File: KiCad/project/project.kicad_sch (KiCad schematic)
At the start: 15 parts, among them P1 Header-Female-2.54_1x3, U1 DRV8313PWPR

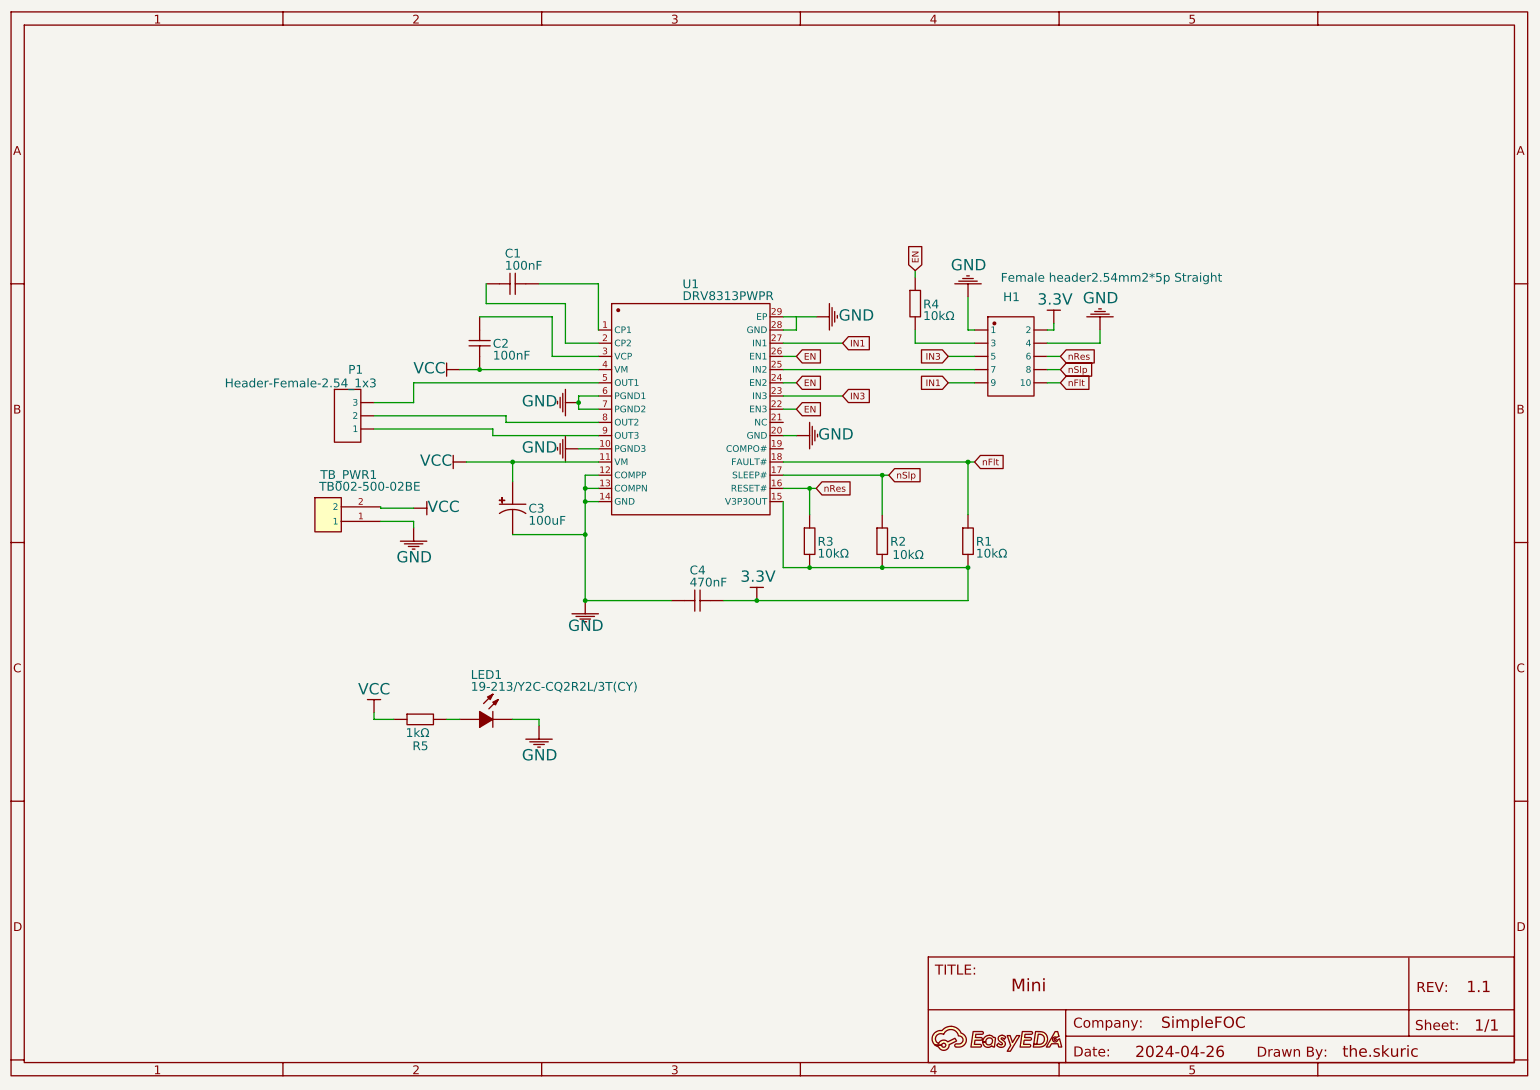
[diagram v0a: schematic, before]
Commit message: Remove imported EasyEDA drawing-frame placeholder from schematic
The EasyEDA import brought in the sheet border/title-block as an
unresolved 291x204mm placeholder symbol (lib_id Unknown_0_-806, ref A1)
wrapping the whole schematic — ~1360 lines / 70KB of non-functional
graphics. KiCad provides its own sheet frame, so it's removed.
Schematic still parses; ERC lib_symbol_issues 30 -> 29.

Co-Authored-By: Claude Opus 4.8 (1M context) <noreply@anthropic.com>
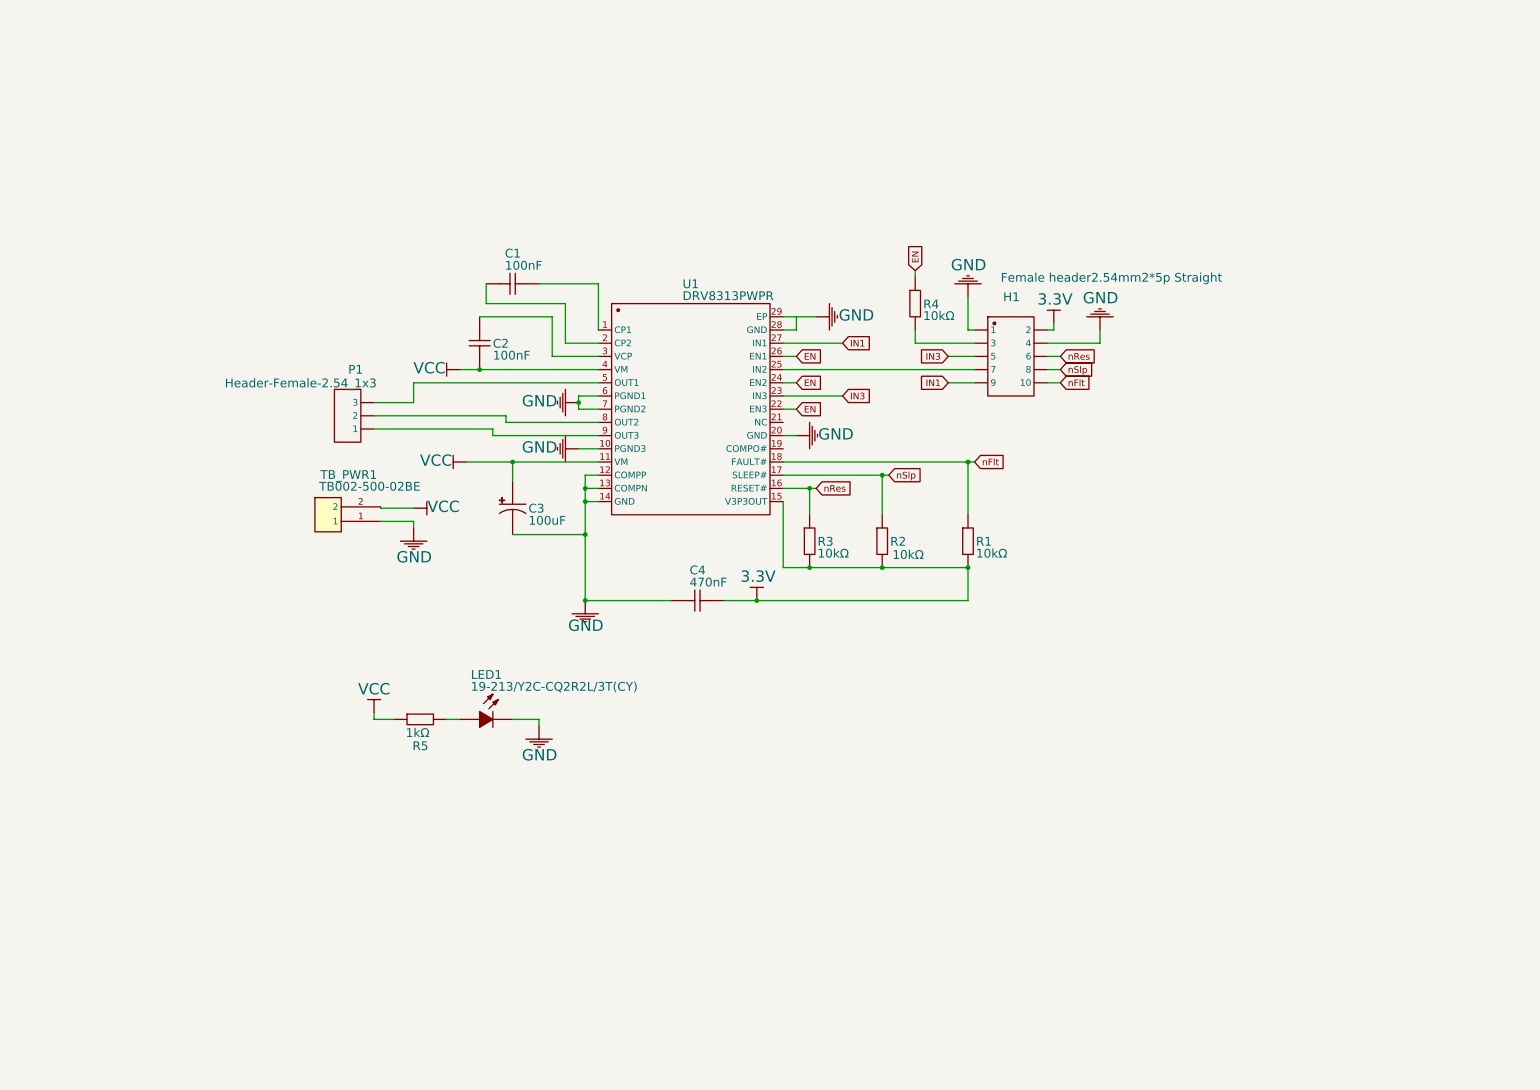
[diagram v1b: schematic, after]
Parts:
- removed A1: A, symbol Unknown_0_-806
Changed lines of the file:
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@@
-		)
-	)
-	(symbol
-		(lib_id "Unknown_0_-806")
-		(at 0 -0.254 0)
-		(unit 0)
-		(body_style 0)
-		(exclude_from_sim no)
-		(in_bom yes)
-		(on_board yes)
-		(in_pos_files yes)
-		(dnp no)
-		(property "Reference" "A1"
-			(at 144.9578 -4.8641 0)
-			(hide yes)
-			(show_name no)
-			(do_not_autoplace no)
-			(effects
-				(font
-					(face "Arial")
-					(size 1.6891 1.6891)
-				)
-				(justify left top)
-			)
-		)
-		(property "Value" "A"
-			(at 144.9578 -2.7051 0)
-			(hide yes)
-			(show_name no)
-			(do_not_autoplace no)
-			(effects
-				(font
-					(face "Arial")
-					(size 1.6891 1.6891)
-				)
-				(justify left top)
-			)
-		)
-		(property "Footprint" ""
-			(at 0 -0.254 0)
-			(hide yes)
-			(show_name no)
-			(do_not_autoplace no)
-			(effects
-				(font
-					(size 1.27 1.27)
-				)
-			)
-		)
-		(property "Datasheet" ""
-			(at 0 -0.254 0)
-			(hide yes)
-			(show_name no)
-			(do_not_autoplace no)
-			(effects
-				(font
-					(size 1.27 1.27)
-				)
-			)
-		)
-		(property "Description" ""
-			(at 0 -0.254 0)
-			(hide yes)
-			(show_name no)
-			(do_not_autoplace no)
-			(effects
-				(font
-					(size 1.27 1.27)
-				)
-			)
-		)
-		(property "Manufacturer Part" "?"
-			(at 0 -0.254 0)
-			(hide yes)
-			(show_name no)
-			(do_not_autoplace no)
-			(effects
-				(font
-					(size 1.27 1.27)
-				)
-			)
-		)
-		(instances
-			(project "project"
-				(path "/03adca04-2da2-4337-bf85-1694768d6810"
-					(reference "A1")
-					(unit 0)
-				)
-			)
 		)
 	)

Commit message: Schematic: mark C3/C1 for 60V; add redesign BOM worklist
- C3 Value -> '100uF 100V', C1 Value -> '100nF 100V' (the two hard-fail
  caps at 60V: VM bulk and charge-pump flying cap). ERC unchanged at 87.
- Left MPN/Supplier-Part fields untouched: the EasyEDA import shares those
  strings across symbols (C1/C2 both carry CL10B104KB8NNNC), so a global
  blank would corrupt siblings. Re-select MPNs per-symbol during rework.
- Add docs/redesign-bom.md: per-reference part-selection worklist with
  status flags. Concrete call: P1 -> TB002-500-03BE (3-pos sibling of
  TB_PWR1's TB002-500-02BE). Open decisions: C1 value (10nF vs 100nF),
  R5 value (1k vs 4.7k), LED1 re-site to 3.3V.
- README + CLAUDE.md updated with schematic/BOM facts.

Co-Authored-By: Claude Opus 4.8 <noreply@anthropic.com>
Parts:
- C1: value 100nF -> 100nF 100V
- C3: value 100uF -> 100uF 100V
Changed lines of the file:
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@@
 			)
 		)
-		(property "Value" "100nF"
+		(property "Value" "100nF 100V"
 			(at 95.0214 47.5869 0)
 			(show_name no)
@@
 			)
 		)
-		(property "Value" "100uF"
+		(property "Value" "100uF 100V"
 			(at 99.568 96.6597 0)
 			(show_name no)

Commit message: Apply cap decisions + re-site LED1 to 3.3V in schematic
- C1 Value -> '10nF 100V' (Samsung C84709, TI datasheet value)
- C3 Value -> '47uF 100V'; bulk is now 2x 47uF/100V parallel (Honor
  C87862) ~= 94uF at full 100V margin (single extended-part fee). C5
  (the parallel twin) to be added during rework.
- LED1 re-sited to the 3.3V rail: swapped power symbol #PWR01 on the R5
  branch from VCC to 3.3V. Verified by netlist export: R5.1 now on net
  3.3V; VCC still carries U1.4/U1.11 (VM). ERC unchanged at 87.
- R5 kept at 1kOhm (~1.3mA indicator on 3.3V).
- redesign-bom.md + CLAUDE.md updated with decisions and remaining work
  (add C5, set per-symbol MPNs, P1 -> TB002-500-03BE footprint).

Co-Authored-By: Claude Opus 4.8 <noreply@anthropic.com>
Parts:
- C1: value 100nF 100V -> 10nF 100V
- C3: value 100uF 100V -> 47uF 100V
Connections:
- net 3.3V: now also R5.1
- net VCC: no longer R5.1
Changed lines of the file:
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@@
 	)
 	(symbol
-		(lib_id "VCC")
+		(lib_id "3.3V")
 		(at 69.85 134.62 0)
 		(mirror x)
@@
 			)
 		)
-		(property "Value" "VCC"
+		(property "Value" "3.3V"
 			(at 66.7766 131.3434 0)
 			(show_name no)
@@
 			)
 		)
-		(property "Value" "100nF 100V"
+		(property "Value" "10nF 100V"
 			(at 95.0214 47.5869 0)
 			(show_name no)
@@
 			)
 		)
-		(property "Value" "100uF 100V"
+		(property "Value" "47uF 100V"
 			(at 99.568 96.6597 0)
 			(show_name no)

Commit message: Schematic: set per-symbol MPNs and add parallel bulk cap C5
Done via anchored text edits (scoped to each symbol instance, safe
against the import's shared part-number strings):
- MPNs set: C1 -> CL10B103KC8NNNC/C84709 (10nF 100V), C3 -> RVT2A470M1010/
  C87862 (47uF 100V), C4 -> CL10B474KA8NNNC/C1623 (470nF 25V X7R),
  R5 -> 0603WAF1001T5E/C21190 (1k, was the 4.7k part).
- C5 added: second 47uF/100V (C87862) in parallel with C3, with its own
  VCC/GND power symbols, on-grid at (96.52, 158.75). Netlist-verified:
  C5.1 on VCC, C5.2 on GND.

ERC 92 (was 87); the +5 are import-category artifacts (lib_symbol_issues
empty-lib, pin_to_pin Unspecified) for the 3 new symbols, which clear
when the symbol libs/pin-types are cleaned up. Remaining is PCB work.

Co-Authored-By: Claude Opus 4.8 <noreply@anthropic.com>
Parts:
- added C5: 47uF 100V, symbol VT1V101M-CRE77
- C1: Manufacturer SAMSUNG -> Samsung; Manufacturer Part CL10B104KB8NNNC -> CL10B103KC8NNNC; Supplier Part C1591 -> C84709
- C3: Manufacturer Vertical Technology -> Honor Elec; Manufacturer Part VT1V101M-CRE77 -> RVT2A470M1010; Supplier Part C294520 -> C87862
- C4: Manufacturer YAGEO -> Samsung; Manufacturer Part CC0603ZRY5V6BB474 -> CL10B474KA8NNNC; Supplier Part C327269 -> C1623
- R5: Manufacturer Part 0603WAF4701T5E -> 0603WAF1001T5E; Supplier Part C23162 -> C21190
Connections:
- net GND: now also C5.2
- net VCC: now also C5.1
